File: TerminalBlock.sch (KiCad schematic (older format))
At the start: 0 parts

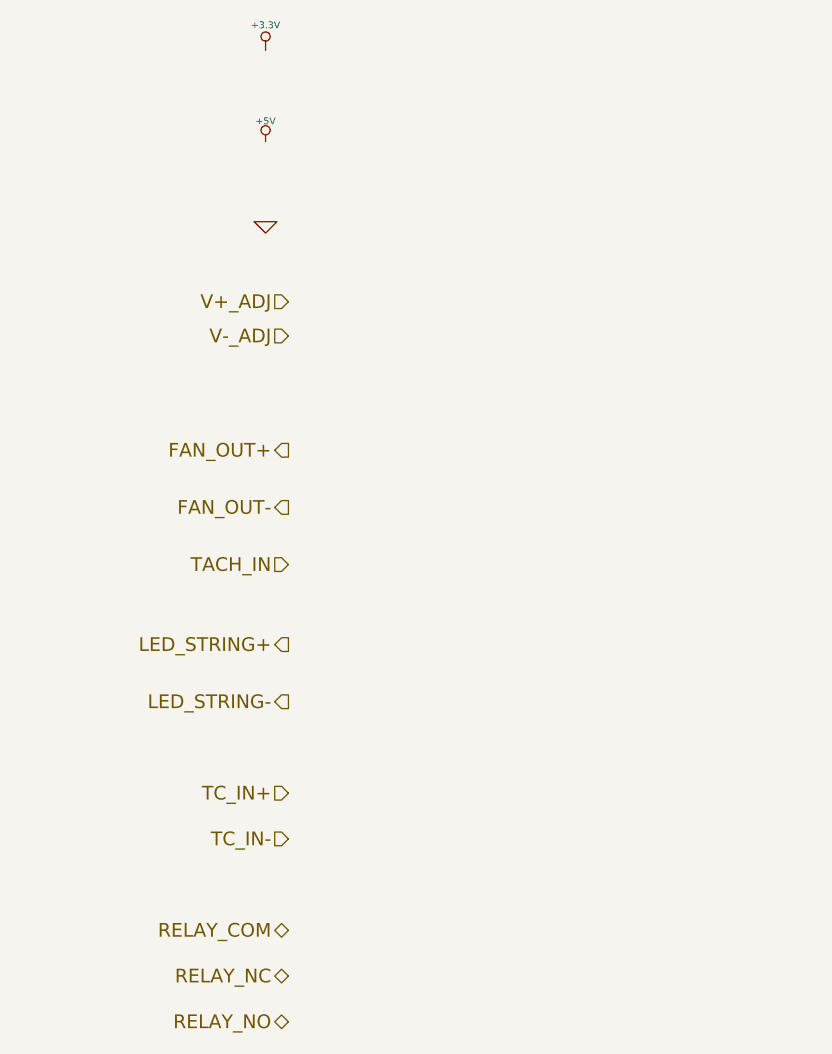
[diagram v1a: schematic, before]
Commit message: Associated and placed thermocouple, terminal, arduino, fan driver, power protection modules.
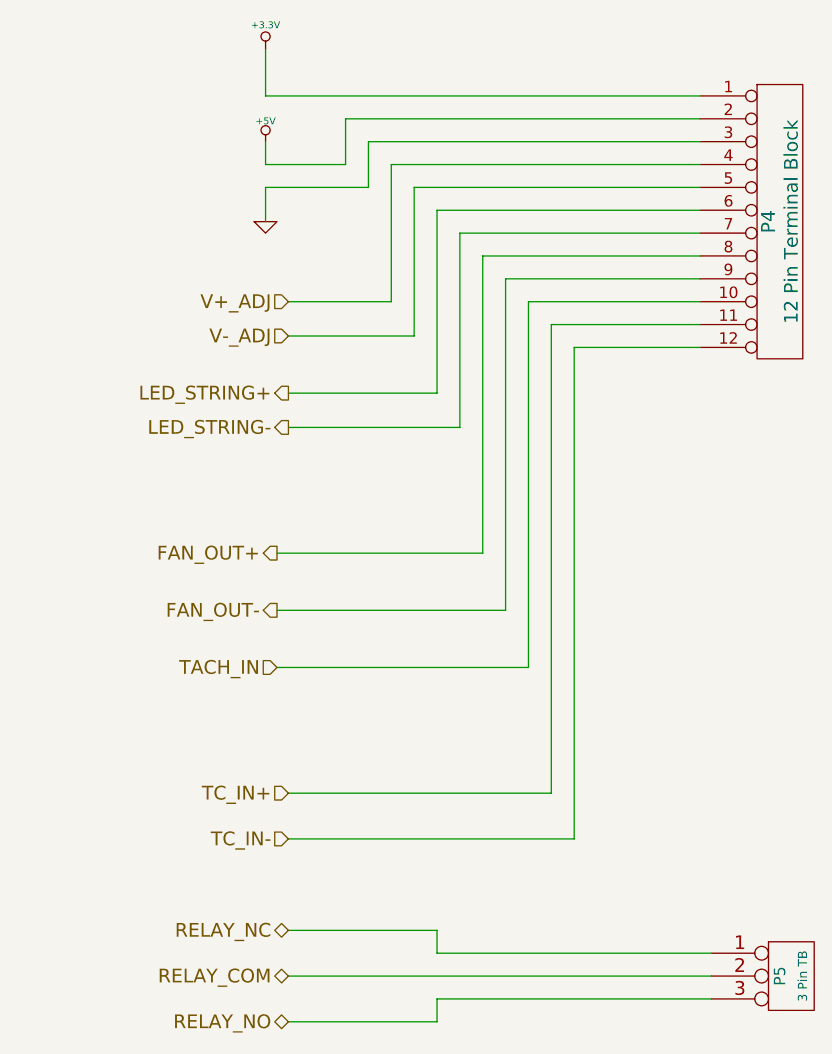
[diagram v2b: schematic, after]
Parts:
- added P4: 12 Pin Terminal Block, symbol CONN_12
- added P5: 3 Pin TB, symbol CONN_3
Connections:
- net +3.3V: now also P4.1 (P1)
- net +5V: now also P4.2 (P2)
- net FAN_OUT+: now also P4.8 (P8)
- net FAN_OUT-: now also P4.9 (P9)
- net GND: now also P4.3 (P3)
- net LED_STRING+: now also P4.6 (P6)
- net LED_STRING-: now also P4.7 (P7)
- net RELAY_COM: now also P5.2 (PM)
- net RELAY_NC: now also P5.1 (P1)
- net RELAY_NO: now also P5.3 (P3)
- net TACH_IN: now also P4.10 (P10)
- net TC_IN+: now also P4.11 (P11)
- net TC_IN-: now also P4.12 (P12)
- net V+_ADJ: now also P4.4 (P4)
- net V-_ADJ: now also P4.5 (P5)
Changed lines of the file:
@@
 $Descr A4 11693 8268
 encoding utf-8
-Sheet 4 9
+Sheet 3 9
 Title ""
 Date ""
@@
 Text HLabel 2150 2100 0    60   Input ~ 0
 V-_ADJ
-Text HLabel 2150 2600 0    60   Output ~ 0
+Text HLabel 2100 3050 0    60   Output ~ 0
 FAN_OUT+
-Text HLabel 2150 2850 0    60   Output ~ 0
+Text HLabel 2100 3300 0    60   Output ~ 0
 FAN_OUT-
-Text HLabel 2150 3100 0    60   Input ~ 0
+Text HLabel 2100 3550 0    60   Input ~ 0
 TACH_IN
-Text HLabel 2150 3450 0    60   Output ~ 0
+Text HLabel 2150 2350 0    60   Output ~ 0
 LED_STRING+
-Text HLabel 2150 3700 0    60   Output ~ 0
+Text HLabel 2150 2500 0    60   Output ~ 0
 LED_STRING-
 Text HLabel 2150 4100 0    60   Input ~ 0
@@
 Text HLabel 2150 4300 0    60   Input ~ 0
 TC_IN-
+Text HLabel 2150 4900 0    60   BiDi ~ 0
+RELAY_COM
 Text HLabel 2150 4700 0    60   BiDi ~ 0
-RELAY_COM
-Text HLabel 2150 4900 0    60   BiDi ~ 0
 RELAY_NC
 Text HLabel 2150 5100 0    60   BiDi ~ 0
 RELAY_NO
 $Comp
-L +3.3V #PWR17
+L +3.3V #PWR056
 U 1 1 52F814D3
 P 2050 850
-F 0 "#PWR17" H 2050 810 30  0001 C CNN
+F 0 "#PWR056" H 2050 810 30  0001 C CNN
 F 1 "+3.3V" H 2050 960 30  0000 C CNN
 F 2 "" H 2050 850 60  0000 C CNN
@@
 $EndComp
 $Comp
-L +5V #PWR18
+L +5V #PWR057
 U 1 1 52F814E7
 P 2050 1250
-F 0 "#PWR18" H 2050 1340 20  0001 C CNN
+F 0 "#PWR057" H 2050 1340 20  0001 C CNN
 F 1 "+5V" H 2050 1340 30  0000 C CNN
 F 2 "" H 2050 1250 60  0000 C CNN
@@
 $EndComp
 $Comp
-L GND #PWR19
+L GND #PWR058
 U 1 1 52F814FB
 P 2050 1600
-F 0 "#PWR19" H 2050 1600 30  0001 C CNN
+F 0 "#PWR058" H 2050 1600 30  0001 C CNN
 F 1 "GND" H 2050 1530 30  0001 C CNN
 F 2 "" H 2050 1600 60  0000 C CNN
@@
 	1    0    0    -1
 $EndComp
+$Comp
+L CONN_12 P4
+U 1 1 5308D90D
+P 4300 1600
+F 0 "P4" V 4250 1600 60  0000 C CNN
+F 1 "12 Pin Terminal Block" V 4350 1600 60  0000 C CNN
+F 2 "" H 4300 1600 60  0000 C CNN
+F 3 "" H 4300 1600 60  0000 C CNN
+F 4 "On Shore" H 4300 1600 60  0001 C CNN "MFG name"
+F 5 "OSTTE120104" H 4300 1600 60  0001 C CNN "MFG Part Number"
+	1    4300 1600
+	1    0    0    -1
+$EndComp
+Wire Wire Line
+	3950 1050 2050 1050
+Wire Wire Line
+	2050 1050 2050 850
+Wire Wire Line
+	3950 1150 2400 1150
+Wire Wire Line
+	2400 1150 2400 1350
+Wire Wire Line
+	2400 1350 2050 1350
+Wire Wire Line
+	2050 1350 2050 1250
+Wire Wire Line
+	3950 1250 2500 1250
+Wire Wire Line
+	2500 1250 2500 1450
+Wire Wire Line
+	2500 1450 2050 1450
+Wire Wire Line
+	2050 1450 2050 1600
+Wire Wire Line
+	3950 1350 2600 1350
+Wire Wire Line
+	2600 1350 2600 1950
+Wire Wire Line
+	2600 1950 2150 1950
+Wire Wire Line
+	3950 1450 2700 1450
+Wire Wire Line
+	2700 1450 2700 2100
+Wire Wire Line
+	2700 2100 2150 2100
+Wire Wire Line
+	3950 1550 2800 1550
+Wire Wire Line
+	2800 1550 2800 2350
+Wire Wire Line
+	2800 2350 2150 2350
+Wire Wire Line
+	3950 1650 2900 1650
+Wire Wire Line
+	2900 1650 2900 2500
+Wire Wire Line
+	2900 2500 2150 2500
+Wire Wire Line
+	3000 1750 3950 1750
+Wire Wire Line
+	3000 1750 3000 3050
+Wire Wire Line
+	3000 3050 2100 3050
+Wire Wire Line
+	3950 1850 3100 1850
+Wire Wire Line
+	3100 1850 3100 3300
+Wire Wire Line
+	3100 3300 2100 3300
+Wire Wire Line
+	3950 1950 3200 1950
+Wire Wire Line
+	3200 1950 3200 3550
+Wire Wire Line
+	3200 3550 2100 3550
+Wire Wire Line
+	3950 2050 3300 2050
+Wire Wire Line
+	3300 2050 3300 4100
+Wire Wire Line
+	3300 4100 2150 4100
+Wire Wire Line
+	3950 2150 3400 2150
+Wire Wire Line
+	3400 2150 3400 4300
+Wire Wire Line
+	3400 4300 2150 4300
+$Comp
+L CONN_3 P5
+U 1 1 5308DD11
+P 4350 4900
+F 0 "P5" V 4300 4900 50  0000 C CNN
+F 1 "3 Pin TB" V 4400 4900 40  0000 C CNN
+F 2 "" H 4350 4900 60  0000 C CNN
+F 3 "" H 4350 4900 60  0000 C CNN
+F 4 "Phoenix Contact" H 4350 4900 60  0001 C CNN "MFG name"
+F 5 "1935174" H 4350 4900 60  0001 C CNN "MFG Part Number"
+	1    4350 4900
+	1    0    0    -1
+$EndComp
+Wire Wire Line
+	2150 4900 4000 4900
+Wire Wire Line
+	4000 4800 2800 4800
+Wire Wire Line
+	2800 4800 2800 4700
+Wire Wire Line
+	2800 4700 2150 4700
+Wire Wire Line
+	4000 5000 2800 5000
+Wire Wire Line
+	2800 5000 2800 5100
+Wire Wire Line
+	2800 5100 2150 5100
 $EndSCHEMATC

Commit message: Layout sessions 1-4.
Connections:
- net GND is gone; now on net TACH_IN: P4.3 (P3)
- net +3.3V: now also P4.10 (P10); no longer P4.1 (P1)
- net +5V: now also P4.9 (P9); no longer P4.2 (P2)
- net FAN_OUT+: now also P4.5 (P5); no longer P4.8 (P8)
- net FAN_OUT-: now also P4.4 (P4); no longer P4.9 (P9)
- net LED_STRING+: now also P4.1 (P1); no longer P4.6 (P6)
- net LED_STRING-: now also P4.2 (P2); no longer P4.7 (P7)
- net RELAY_NC: now also P5.3 (P3); no longer P5.1 (P1)
- net RELAY_NO: now also P5.1 (P1); no longer P5.3 (P3)
- net TACH_IN: no longer P4.10 (P10)
- net TC_IN+: now also P4.7 (P7); no longer P4.11 (P11)
- net TC_IN-: now also P4.6 (P6); no longer P4.12 (P12)
- net V+_ADJ: now also P4.12 (P12); no longer P4.4 (P4)
- net V-_ADJ: now also P4.11 (P11); no longer P4.5 (P5)
- new net GND_PWR: P4.8 (P8)
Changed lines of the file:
@@
 $Descr A4 11693 8268
 encoding utf-8
-Sheet 3 9
+Sheet 8 9
 Title ""
 Date ""
@@
 Comment4 ""
 $EndDescr
-Text HLabel 2150 1950 0    60   Input ~ 0
+Text HLabel 2150 4300 0    60   Input ~ 0
 V+_ADJ
-Text HLabel 2150 2100 0    60   Input ~ 0
+Text HLabel 2150 4100 0    60   Input ~ 0
 V-_ADJ
-Text HLabel 2100 3050 0    60   Output ~ 0
+Text HLabel 2400 2250 0    60   Output ~ 0
 FAN_OUT+
-Text HLabel 2100 3300 0    60   Output ~ 0
+Text HLabel 2350 1950 0    60   Output ~ 0
 FAN_OUT-
-Text HLabel 2100 3550 0    60   Input ~ 0
+Text HLabel 2050 1450 0    60   Input ~ 0
 TACH_IN
-Text HLabel 2150 2350 0    60   Output ~ 0
+Text HLabel 1750 1050 0    60   Output ~ 0
 LED_STRING+
-Text HLabel 2150 2500 0    60   Output ~ 0
+Text HLabel 1750 1150 0    60   Output ~ 0
 LED_STRING-
-Text HLabel 2150 4100 0    60   Input ~ 0
+Text HLabel 2400 2800 0    60   Input ~ 0
 TC_IN+
-Text HLabel 2150 4300 0    60   Input ~ 0
+Text HLabel 2400 2600 0    60   Input ~ 0
 TC_IN-
 Text HLabel 2150 4900 0    60   BiDi ~ 0
 RELAY_COM
+Text HLabel 2150 5100 0    60   BiDi ~ 0
+RELAY_NC
 Text HLabel 2150 4700 0    60   BiDi ~ 0
-RELAY_NC
-Text HLabel 2150 5100 0    60   BiDi ~ 0
 RELAY_NO
 $Comp
-L +3.3V #PWR056
+L +3.3V #PWR047
 U 1 1 52F814D3
-P 2050 850
-F 0 "#PWR056" H 2050 810 30  0001 C CNN
-F 1 "+3.3V" H 2050 960 30  0000 C CNN
-F 2 "" H 2050 850 60  0000 C CNN
-F 3 "" H 2050 850 60  0000 C CNN
-	1    2050 850
+P 1150 3400
+F 0 "#PWR047" H 1150 3360 30  0001 C CNN
+F 1 "+3.3V" H 1150 3510 30  0000 C CNN
+F 2 "" H 1150 3400 60  0000 C CNN
+F 3 "" H 1150 3400 60  0000 C CNN
+	1    1150 3400
 	1    0    0    -1
 $EndComp
 $Comp
-L +5V #PWR057
+L +5V #PWR048
 U 1 1 52F814E7
-P 2050 1250
-F 0 "#PWR057" H 2050 1340 20  0001 C CNN
-F 1 "+5V" H 2050 1340 30  0000 C CNN
-F 2 "" H 2050 1250 60  0000 C CNN
-F 3 "" H 2050 1250 60  0000 C CNN
-	1    2050 1250
-	1    0    0    -1
-$EndComp
-$Comp
-L GND #PWR058
-U 1 1 52F814FB
-P 2050 1600
-F 0 "#PWR058" H 2050 1600 30  0001 C CNN
-F 1 "GND" H 2050 1530 30  0001 C CNN
-F 2 "" H 2050 1600 60  0000 C CNN
-F 3 "" H 2050 1600 60  0000 C CNN
-	1    2050 1600
+P 1750 3200
+F 0 "#PWR048" H 1750 3290 20  0001 C CNN
+F 1 "+5V" H 1750 3290 30  0000 C CNN
+F 2 "" H 1750 3200 60  0000 C CNN
+F 3 "" H 1750 3200 60  0000 C CNN
+	1    1750 3200
 	1    0    0    -1
 $EndComp
@@
 $EndComp
 Wire Wire Line
-	3950 1050 2050 1050
+	1150 3550 1150 3400
 Wire Wire Line
-	2050 1050 2050 850
+	1750 1150 3950 1150
 Wire Wire Line
-	3950 1150 2400 1150
+	1750 3300 3100 3300
 Wire Wire Line
-	2400 1150 2400 1350
-Wire Wire Line
-	2400 1350 2050 1350
-Wire Wire Line
-	2050 1350 2050 1250
+	1750 3300 1750 3200
 Wire Wire Line
 	3950 1250 2500 1250
@@
 	2500 1450 2050 1450
 Wire Wire Line
-	2050 1450 2050 1600
+	2200 3050 2200 3200
 Wire Wire Line
 	3950 1350 2600 1350
@@
 	2600 1350 2600 1950
 Wire Wire Line
-	2600 1950 2150 1950
-Wire Wire Line
 	3950 1450 2700 1450
 Wire Wire Line
-	2700 1450 2700 2100
-Wire Wire Line
-	2700 2100 2150 2100
+	2700 1450 2700 2250
 Wire Wire Line
 	3950 1550 2800 1550
 Wire Wire Line
-	2800 1550 2800 2350
+	2800 1550 2800 2600
 Wire Wire Line
-	2800 2350 2150 2350
+	1750 1050 3950 1050
 Wire Wire Line
 	3950 1650 2900 1650
 Wire Wire Line
-	2900 1650 2900 2500
-Wire Wire Line
-	2900 2500 2150 2500
+	2900 1650 2900 2800
 Wire Wire Line
 	3000 1750 3950 1750
 Wire Wire Line
-	3000 1750 3000 3050
+	3000 3050 3000 1750
 Wire Wire Line
-	3000 3050 2100 3050
+	2200 3050 3000 3050
 Wire Wire Line
 	3950 1850 3100 1850
@@
 	3100 1850 3100 3300
 Wire Wire Line
-	3100 3300 2100 3300
-Wire Wire Line
 	3950 1950 3200 1950
 Wire Wire Line
 	3200 1950 3200 3550
 Wire Wire Line
-	3200 3550 2100 3550
+	3200 3550 1150 3550
 Wire Wire Line
 	3950 2050 3300 2050
@@
 Wire Wire Line
 	2800 5100 2150 5100
+Wire Wire Line
+	2600 1950 2350 1950
+Wire Wire Line
+	2700 2250 2400 2250
+Wire Wire Line
+	2900 2800 2400 2800
+Wire Wire Line
+	2800 2600 2400 2600
+$Comp
+L GND_PWR #PWR049
+U 1 1 5313EDAA
+P 2200 3200
+F 0 "#PWR049" H 2200 3200 30  0001 C CNN
+F 1 "GND_PWR" H 2200 3130 30  0000 C CNN
+F 2 "" H 2200 3200 60  0000 C CNN
+F 3 "" H 2200 3200 60  0000 C CNN
+	1    2200 3200
+	1    0    0    -1
+$EndComp
 $EndSCHEMATC
